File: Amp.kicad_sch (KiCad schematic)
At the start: 28 parts

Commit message: Some updates
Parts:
- added C5: 22u 63v, Capacitor_THT:CP_Radial_D6.3mm_P2.50mm, symbol Device:C_Polarized
- added C8, C?: 470u 600v, Capacitor_THT:CP_Radial_D40.0mm_P10.00mm_SnapIn, symbol Device:C_Polarized
- added C9: 4n7 600v, Capacitor_THT:C_Rect_L16.5mm_W5.0mm_P15.00mm_MKT, symbol Device:C
- added D1: D_Bridge_+-AA, Diode_THT:Diode_Bridge_32.0x5.6x17.0mm_P10.0mm_P7.5mm, symbol Device:D_Bridge_+-AA
- added F1: Fuse, symbol Device:Fuse
- added R16: 220k 2W, Resistor_THT:R_Axial_DIN0516_L15.5mm_D5.0mm_P20.32mm_Horizontal, symbol Device:R
- added R8: 10k 2W, symbol Device:R
- C1, C3, C4: renamed from C?; value C -> 220n 400v; footprint (none) -> Capacitor_THT:C_Rect_L16.5mm_W5.0mm_P15.00mm_MKT
- C2: renamed from C?; value C -> 220n 400v
- C6, C7: renamed from C?; value C -> 220u 63v; footprint (none) -> Capacitor_THT:C_Radial_D10.0mm_H16.0mm_P5.00mm; symbol Device:C -> Device:C_Polarized
- P1: renamed from RV?; value R_Potentiometer -> 100k; footprint (none) -> Potentiometer_THT:Potentiometer_TT_P0915N
- R1: renamed from R?; value R -> 22k 1W; footprint (none) -> Resistor_THT:R_Axial_DIN0414_L11.9mm_D4.5mm_P20.32mm_Horizontal
- R10, R9: renamed from R?; value R -> 1k5 1W; footprint (none) -> Resistor_THT:R_Axial_DIN0414_L11.9mm_D4.5mm_P20.32mm_Horizontal
- R11, R12: renamed from R?; value R -> 330 5W; footprint (none) -> Resistor_THT:R_Axial_Power_L25.0mm_W6.4mm_P30.48mm
- R13, R14, R15: renamed from R?; value R -> 470 1W; footprint (none) -> Resistor_THT:R_Axial_DIN0414_L11.9mm_D4.5mm_P20.32mm_Horizontal
- R2, R3: renamed from R?; value R -> 1M5 1W; footprint (none) -> Resistor_THT:R_Axial_DIN0414_L11.9mm_D4.5mm_P20.32mm_Horizontal
- R4, R5: renamed from R?; value R -> 100k 1W; footprint (none) -> Resistor_THT:R_Axial_DIN0414_L11.9mm_D4.5mm_P20.32mm_Horizontal
- R6, R7: renamed from R?; value R -> 470k 1W; footprint (none) -> Resistor_THT:R_Axial_DIN0414_L11.9mm_D4.5mm_P20.32mm_Horizontal
- gave numbers to parts that had none: 3
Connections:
- net GND: now also C2.1, C6.2, C5.2, C9.1, C?.2, D1.2 (-), R16.2; no longer C6.1
- net at R11.1, U2.1 (G3), U2.8 (F1): now also C6.1; no longer C6.2
- net +A2: now reaches R4.2, R5.1
- net +A2: now also C5.1, R8.1
- new net: C8.2, C?.1
- new net: D1.3, F1.1
- new net +A: C8.1, C9.2, D1.1 (+), R16.1, R8.2
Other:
- moved on the sheet: C1, C2, C3, C4, P1, R1, R10, R11, R12, R13, R14, R15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

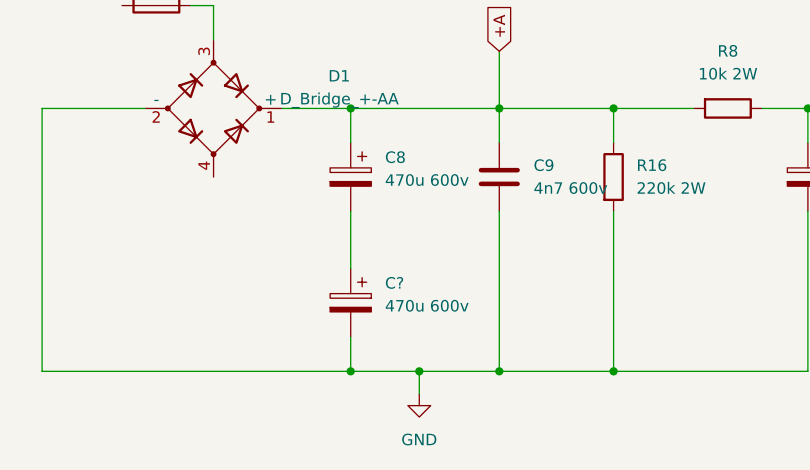
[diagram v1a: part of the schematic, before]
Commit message: Adding footprints
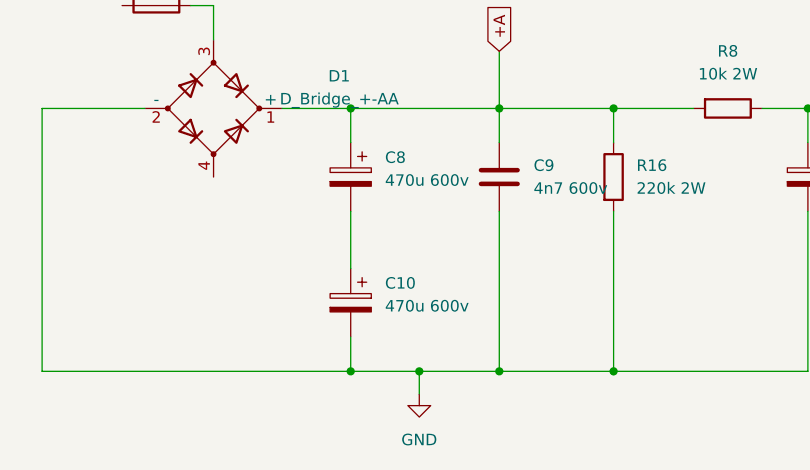
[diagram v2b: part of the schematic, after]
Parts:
- C2: footprint (none) -> Capacitor_THT:C_Rect_L16.5mm_W5.0mm_P15.00mm_MKT
- R8: footprint (none) -> Resistor_THT:R_Axial_DIN0516_L15.5mm_D5.0mm_P20.32mm_Horizontal
- gave numbers to parts that had none: 1
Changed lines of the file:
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@@
       (effects (font (size 1.27 1.27)) (justify right))
     )
-    (property "Footprint" "" (id 2) (at 113.3348 86.36 0)
+    (property "Footprint" "Capacitor_THT:C_Rect_L16.5mm_W5.0mm_P15.00mm_MKT" (id 2) (at 113.3348 86.36 0)
       (effects (font (size 1.27 1.27)) hide)
     )
@@
   (symbol (lib_id "Device:C_Polarized") (at 68.58 161.29 0) (mirror y) (unit 1)
     (in_bom yes) (on_board yes) (fields_autoplaced)
-    (property "Reference" "C?" (id 0) (at 72.39 159.1309 0)
+    (property "Reference" "C10" (id 0) (at 72.39 159.1309 0)
       (effects (font (size 1.27 1.27)) (justify right))
     )
@@
     (property "Reference" "R8" (id 0) (at 110.49 133.35 90))
     (property "Value" "10k 2W" (id 1) (at 110.49 135.89 90))
-    (property "Footprint" "" (id 2) (at 110.49 137.922 90)
+    (property "Footprint" "Resistor_THT:R_Axial_DIN0516_L15.5mm_D5.0mm_P20.32mm_Horizontal" (id 2) (at 110.49 137.922 90)
       (effects (font (size 1.27 1.27)) hide)
     )
@@
     )
     (path "/92ee6384-95e9-4a05-9421-6294b3081d53"
-      (reference "C2") (unit 1) (value "220n 400v") (footprint "")
+      (reference "C2") (unit 1) (value "220n 400v") (footprint "Capacitor_THT:C_Rect_L16.5mm_W5.0mm_P15.00mm_MKT")
     )
     (path "/64c6b567-6f34-481a-af3b-20efa7fb7043"
@@
     )
     (path "/d2e16e45-6d4a-46bd-9ebc-a353f743c593"
-      (reference "C?") (unit 1) (value "470u 600v") (footprint "Capacitor_THT:CP_Radial_D40.0mm_P10.00mm_SnapIn")
+      (reference "C10") (unit 1) (value "470u 600v") (footprint "Capacitor_THT:CP_Radial_D40.0mm_P10.00mm_SnapIn")
     )
     (path "/aa2ac28d-003c-48fd-acd1-496425f21c44"
@@
     )
     (path "/ed25f9cd-445d-4a9f-af51-0317ad1d76af"
-      (reference "R8") (unit 1) (value "10k 2W") (footprint "")
+      (reference "R8") (unit 1) (value "10k 2W") (footprint "Resistor_THT:R_Axial_DIN0516_L15.5mm_D5.0mm_P20.32mm_Horizontal")
     )
     (path "/8d921e63-bec9-4a36-a0fb-640e2174fa00"

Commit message: Update
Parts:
- added J1, J3, J4, J5: Screw_Terminal_01x02, Connector:Banana_Jack_2Pin, symbol Connector:Screw_Terminal_01x02
- added J2: AudioJack2, Connector_Audio:Jack_3.5mm_CUI_SJ-3523-SMT_Horizontal, symbol Connector:AudioJack2
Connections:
- net +A: now also J4.1 (Pin_1)
- net GND: now also J2.T, J4.2 (Pin_2)
- net at R14.1: now also J3.2 (Pin_2)
- net at R13.1: now also J5.1 (Pin_1)
- net at U3.3 (A): now also J5.2 (Pin_2)
- net at P1.1: now also J2.S
- net at D1.4: now also J1.1 (Pin_1)
- net at F1.2: now also J1.2 (Pin_2)
- net at U2.3 (A): now also J3.1 (Pin_1)

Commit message: Update
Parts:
- removed J1, J3, J4, J5: Screw_Terminal_01x02, Connector:Banana_Jack_2Pin, symbol Connector:Screw_Terminal_01x02
- added F? (x3): Fuse, Fuse:Fuseholder_Cylinder-5x20mm_Schurter_0031_8201_Horizontal_Open, symbol Device:Fuse
- added J1, J3, J4, J5, J6, J7, J8, J9, J? (x5): Conn_01x01_Female, Connector_Pin:Pin_D1.0mm_L10.0mm, symbol Connector:Conn_01x01_Female
- F1: footprint (none) -> Fuse:Fuseholder_Cylinder-5x20mm_Schurter_0031_8201_Horizontal_Open
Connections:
- net +A: now also J6.1 (Pin_1)
- net GND: now also J7.1 (Pin_1)
- net at D1.4: now also J4.1 (Pin_1)
- net at F1.2: now also J3.1 (Pin_1)
- net at U1.4 (F1): now also J?.1 (Pin_1)
- net at U1.5 (F1): now also J?.1 (Pin_1)
- net at U1.9 (F2): now also F?.1
- net at R14.1: now also J5.1 (Pin_1)
- net at R13.1: now also J8.1 (Pin_1)
- net at U2.3 (A): now also J1.1 (Pin_1)
- net at U3.3 (A): now also J9.1 (Pin_1)
- net at U2.2 (F1): now also F?.1
- net at U2.7 (F2): now also J?.1 (Pin_1)
- net at U3.2 (F1): now also F?.1
- net at U3.7 (F2): now also J?.1 (Pin_1)
- new net: F?.2, J?.1 (Pin_1)
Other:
- moved on the sheet: U1C, U2B, U3B

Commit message: Update
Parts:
- gave numbers to parts that had none: 8
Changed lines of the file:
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@@
   (symbol (lib_id "Device:Fuse") (at 186.69 139.7 0) (unit 1)
     (in_bom yes) (on_board yes) (fields_autoplaced)
-    (property "Reference" "F?" (id 0) (at 189.23 138.4299 0)
+    (property "Reference" "F3" (id 0) (at 189.23 138.4299 0)
       (effects (font (size 1.27 1.27)) (justify left))
     )
@@
   (symbol (lib_id "Device:Fuse") (at 204.47 139.7 0) (unit 1)
     (in_bom yes) (on_board yes) (fields_autoplaced)
-    (property "Reference" "F?" (id 0) (at 207.01 138.4299 0)
+    (property "Reference" "F4" (id 0) (at 207.01 138.4299 0)
       (effects (font (size 1.27 1.27)) (justify left))
     )
@@
   (symbol (lib_id "Connector:Conn_01x01_Female") (at 170.18 148.59 270) (unit 1)
     (in_bom yes) (on_board yes) (fields_autoplaced)
-    (property "Reference" "J?" (id 0) (at 171.45 146.6849 90)
+    (property "Reference" "J11" (id 0) (at 171.45 146.6849 90)
       (effects (font (size 1.27 1.27)) (justify left))
     )
@@
   (symbol (lib_id "Device:Fuse") (at 170.18 139.7 0) (unit 1)
     (in_bom yes) (on_board yes) (fields_autoplaced)
-    (property "Reference" "F?" (id 0) (at 172.72 138.4299 0)
+    (property "Reference" "F2" (id 0) (at 172.72 138.4299 0)
       (effects (font (size 1.27 1.27)) (justify left))
     )
@@
   (symbol (lib_id "Connector:Conn_01x01_Female") (at 167.64 140.97 270) (unit 1)
     (in_bom yes) (on_board yes) (fields_autoplaced)
-    (property "Reference" "J?" (id 0) (at 168.91 139.0649 90)
+    (property "Reference" "J10" (id 0) (at 168.91 139.0649 90)
       (effects (font (size 1.27 1.27)) (justify left))
     )
@@
   (symbol (lib_id "Connector:Conn_01x01_Female") (at 209.55 140.97 270) (unit 1)
     (in_bom yes) (on_board yes) (fields_autoplaced)
-    (property "Reference" "J?" (id 0) (at 210.82 139.0649 90)
+    (property "Reference" "J14" (id 0) (at 210.82 139.0649 90)
       (effects (font (size 1.27 1.27)) (justify left))
     )
@@
   (symbol (lib_id "Connector:Conn_01x01_Female") (at 191.77 140.97 270) (unit 1)
     (in_bom yes) (on_board yes) (fields_autoplaced)
-    (property "Reference" "J?" (id 0) (at 193.04 139.0649 90)
+    (property "Reference" "J13" (id 0) (at 193.04 139.0649 90)
       (effects (font (size 1.27 1.27)) (justify left))
     )
@@
   (symbol (lib_id "Connector:Conn_01x01_Female") (at 172.72 140.97 270) (unit 1)
     (in_bom yes) (on_board yes) (fields_autoplaced)
-    (property "Reference" "J?" (id 0) (at 173.99 139.0649 90)
+    (property "Reference" "J12" (id 0) (at 173.99 139.0649 90)
       (effects (font (size 1.27 1.27)) (justify left))
     )
@@
       (reference "F1") (unit 1) (value "Fuse") (footprint "Fuse:Fuseholder_Cylinder-5x20mm_Schurter_0031_8201_Horizontal_Open")
     )
+    (path "/a1adcb6c-db44-4b49-93cb-68ae942fb387"
+      (reference "F2") (unit 1) (value "Fuse") (footprint "Fuse:Fuseholder_Cylinder-5x20mm_Schurter_0031_8201_Horizontal_Open")
+    )
     (path "/25fbb172-8ec9-4c95-8bc3-97f4ffc44970"
-      (reference "F?") (unit 1) (value "Fuse") (footprint "Fuse:Fuseholder_Cylinder-5x20mm_Schurter_0031_8201_Horizontal_Open")
+      (reference "F3") (unit 1) (value "Fuse") (footprint "Fuse:Fuseholder_Cylinder-5x20mm_Schurter_0031_8201_Horizontal_Open")
     )
     (path "/6e05b8a2-376d-4b46-b83d-ba7e6ff52c0c"
-      (reference "F?") (unit 1) (value "Fuse") (footprint "Fuse:Fuseholder_Cylinder-5x20mm_Schurter_0031_8201_Horizontal_Open")
-    )
-    (path "/a1adcb6c-db44-4b49-93cb-68ae942fb387"
-      (reference "F?") (unit 1) (value "Fuse") (footprint "Fuse:Fuseholder_Cylinder-5x20mm_Schurter_0031_8201_Horizontal_Open")
+      (reference "F4") (unit 1) (value "Fuse") (footprint "Fuse:Fuseholder_Cylinder-5x20mm_Schurter_0031_8201_Horizontal_Open")
     )
     (path "/61c97752-6da3-4341-ab98-f5445eac9c73"
@@
       (reference "J9") (unit 1) (value "Conn_01x01_Female") (footprint "Connector_Pin:Pin_D1.0mm_L10.0mm")
     )
+    (path "/b5815324-6ba2-42f0-9780-104e90daf288"
+      (reference "J10") (unit 1) (value "Conn_01x01_Female") (footprint "Connector_Pin:Pin_D1.0mm_L10.0mm")
+    )
     (path "/72a3e0c6-7ea5-445a-8b6e-f4f233fb6743"
-      (reference "J?") (unit 1) (value "Conn_01x01_Female") (footprint "Connector_Pin:Pin_D1.0mm_L10.0mm")
-    )
-    (path "/b5815324-6ba2-42f0-9780-104e90daf288"
-      (reference "J?") (unit 1) (value "Conn_01x01_Female") (footprint "Connector_Pin:Pin_D1.0mm_L10.0mm")
+      (reference "J11") (unit 1) (value "Conn_01x01_Female") (footprint "Connector_Pin:Pin_D1.0mm_L10.0mm")
+    )
+    (path "/f0993887-d724-43e0-a22c-a1c622282bd8"
+      (reference "J12") (unit 1) (value "Conn_01x01_Female") (footprint "Connector_Pin:Pin_D1.0mm_L10.0mm")
+    )
+    (path "/e48ab2ba-f66f-4a03-9892-4352a1c7ac9f"
+      (reference "J13") (unit 1) (value "Conn_01x01_Female") (footprint "Connector_Pin:Pin_D1.0mm_L10.0mm")
     )
     (path "/b6988044-dd27-4444-9c1d-a6a06e5158f8"
-      (reference "J?") (unit 1) (value "Conn_01x01_Female") (footprint "Connector_Pin:Pin_D1.0mm_L10.0mm")
-    )
-    (path "/e48ab2ba-f66f-4a03-9892-4352a1c7ac9f"
-      (reference "J?") (unit 1) (value "Conn_01x01_Female") (footprint "Connector_Pin:Pin_D1.0mm_L10.0mm")
-    )
-    (path "/f0993887-d724-43e0-a22c-a1c622282bd8"
-      (reference "J?") (unit 1) (value "Conn_01x01_Female") (footprint "Connector_Pin:Pin_D1.0mm_L10.0mm")
+      (reference "J14") (unit 1) (value "Conn_01x01_Female") (footprint "Connector_Pin:Pin_D1.0mm_L10.0mm")
     )
     (path "/83260ffb-4f0b-4387-910e-aee74b14be4e"

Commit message: Update, cleanup
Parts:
- added J15, J16, J17: Conn_01x01_Female, Connector_Pin:Pin_D1.0mm_L10.0mm, symbol Connector:Conn_01x01_Female
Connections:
- net Earth: now also J17.1 (Pin_1)
- net at F3.2: now also J15.1 (Pin_1)
- net at F4.2: now also J16.1 (Pin_1)
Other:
- moved on the sheet: C1, C10, C2, C3, C4, C5, C6, C7, C8, C9, D1, F1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
